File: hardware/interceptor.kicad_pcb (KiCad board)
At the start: 2 copper layers, 78.9 x 59.7 mm, 32 parts, among them IC1 ATMEGA1284P-P, K1 USB, P1 TAPEPORT, P2 CIA1, P3 KEYBOARD, P4 USER A, P5 USER B, SW1 RESET, SW2 BOOTLOADER, U1 7400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

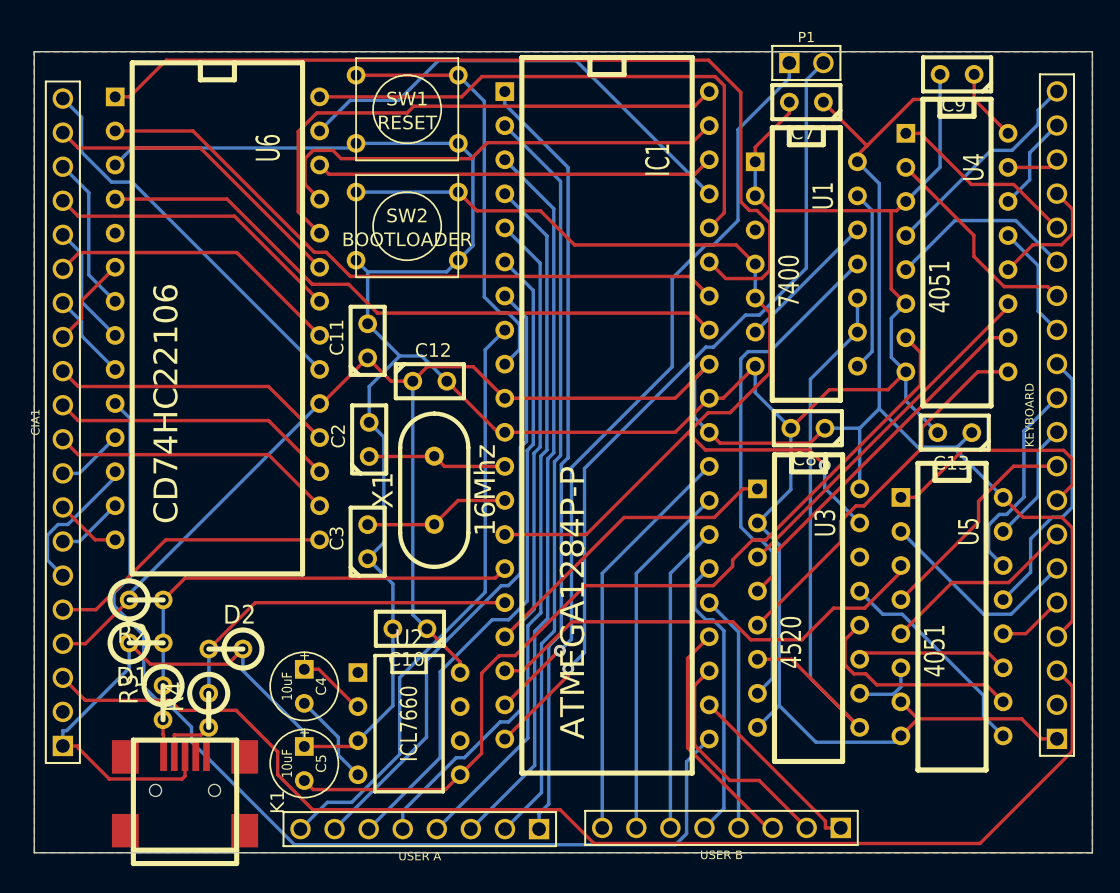
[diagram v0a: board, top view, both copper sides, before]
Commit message: Hardware: Fixed Crosspoint switch and usb connector, routed usb traces
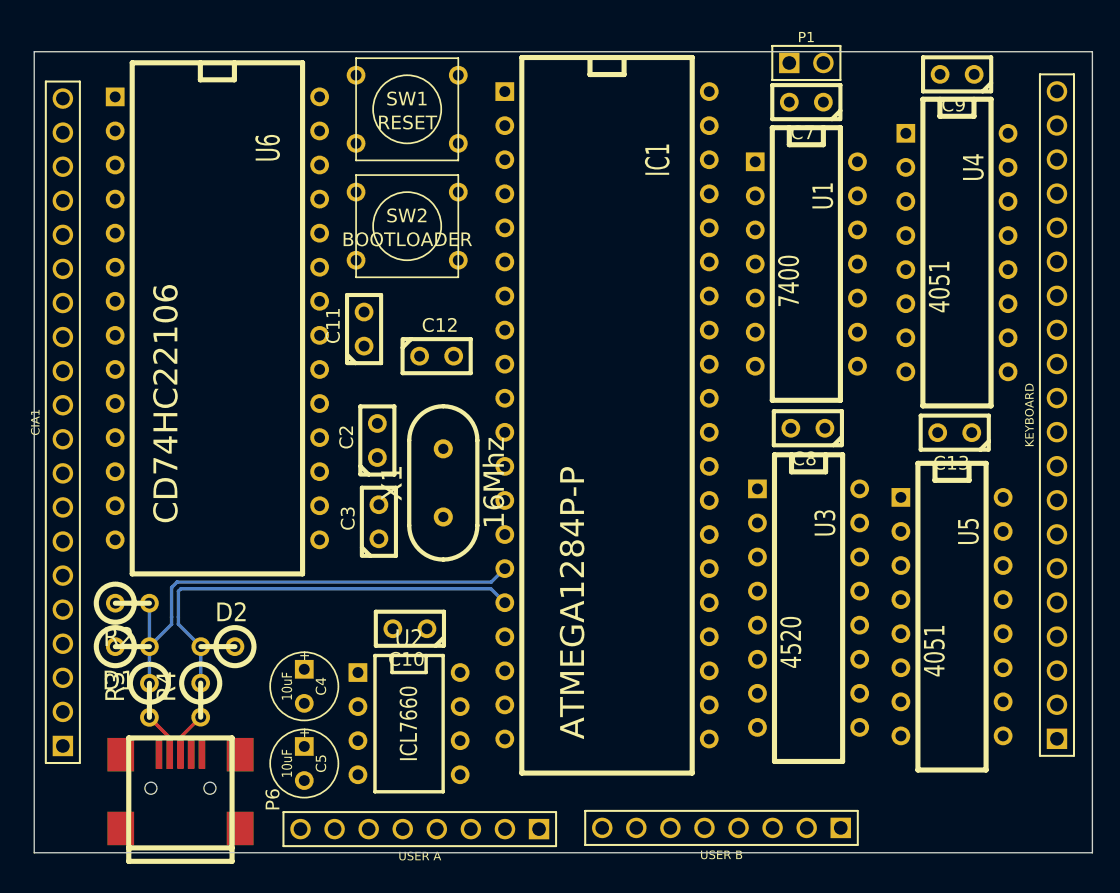
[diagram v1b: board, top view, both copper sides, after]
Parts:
- removed K1: USB, USB_MINI_B
- added P6: USB, USB_MINI_B_CORRECTED, F.Cu at (24.4, 88.6)
- moved C12 1.93 mm to (43.5, 55.5)
- moved C3 1.71 mm to (39.2, 67.9)
- moved D1 1.07 mm to (20.8, 77.2)
- moved R2 1.06 mm to (20.8, 73.9)
- moved R3 1.03 mm to (22.1, 81.2)
- moved R4 0.97 mm to (25.9, 81.2)
- moved C11 0.92 mm to (38.1, 53.5)
- moved X1 0.87 mm to (44.0, 65.0)
- moved D2 0.62 mm to (27.2, 77.2)
- moved C2 0.61 mm to (39.1, 61.8)
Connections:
- U6 pad 5: (no net) -> GND
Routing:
- net GND: track 280.1 -> 0.00 mm
- net VCC: track 176.6 -> 0.00 mm
- net /~RESTORE: track 90.7 -> 0.00 mm
- net /MR: track 81.9 -> 0.00 mm, vias 1 -> 0
- net /~CPMR: track 77.1 -> 0.00 mm
- net /CPA5: track 68.5 -> 0.00 mm
- net /VEE: track 66.5 -> 0.00 mm
- net /CD: track 61.2 -> 0.00 mm, vias 1 -> 0
- net /UA0: track 57.9 -> 0.00 mm
- net /CS: track 57.0 -> 0.00 mm, vias 1 -> 0
- net /UA1: track 55.9 -> 0.00 mm
- net /UA2: track 54.0 -> 0.00 mm
- net /UA3: track 52.1 -> 0.00 mm
- net /UA4: track 50.9 -> 0.00 mm
- net /~CPS: track 49.4 -> 0.00 mm
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- removed copper zone on B.Cu, net GND
- removed copper zone on F.Cu, net GND

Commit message: Hardware: First serious draft of pcb layout
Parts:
- removed C13, C7, C8, C9: 100nF, C1
- removed P5: USER B, pinHeader-8x1
- added JP1: JUMPER, PIN_ARRAY_2X1, F.Cu at (16.2, 89.1)
- C4, C5: footprint C1V5 -> CR2H11W5H
- P4: value USER A -> USER; footprint pinHeader-8x1 -> pin_array_8x2
- moved P1 57.6 mm to (57.0, 89.6), turned to 180 degrees
- moved P4 35.2 mm to (77.3, 86.9)
- moved R3 16.7 mm to (38.8, 80.9)
- moved D1 16.7 mm to (37.5, 76.9)
- moved D2 16.7 mm to (43.9, 76.9)
- moved P6 16.7 mm to (41.1, 88.3)
- moved R4 16.7 mm to (42.6, 80.9)
- moved R2 15.7 mm to (36.5, 73.4)
- moved C4 13.4 mm to (21.3, 85.2), turned to 180 degrees
- moved C10 12.5 mm to (29.4, 72.7)
- moved U2 12.3 mm to (29.5, 80.1)
- moved U5 6.50 mm to (83.0, 68.5)
- moved U3 5.82 mm to (72.0, 68.5)
- moved U1 5.25 mm to (72.0, 43.5)
- moved C5 4.30 mm to (31.0, 89.3)
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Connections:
- P2 pad 4: VCC -> /EXTVCC
- P3 pad 4: VCC -> (no net)
- P4 pad 2: /UA1 -> /UB0
- P4 pad 3: /UA2 -> /UA1
- P4 pad 4: /UA3 -> /UB1
- P4 pad 5: /UA4 -> /UA2
- P4 pad 6: /UA5 -> /UB2
- P4 pad 7: /UA6 -> /UA3
- P4 pad 8: /UA7 -> /UB3
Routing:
- net GND: track 0.00 -> 280.5 mm
- net VCC: track 0.00 -> 155.8 mm
- net /~RESTORE: track 0.00 -> 88.5 mm, vias 0 -> 1
- net /VEE: track 0.00 -> 84.8 mm, vias 0 -> 3
- net /MR: track 0.00 -> 83.7 mm, vias 0 -> 1
- net /UA0: track 0.00 -> 76.7 mm
- net /UA1: track 0.00 -> 71.8 mm
- net /MD: track 0.00 -> 70.6 mm
- net /UA2: track 0.00 -> 69.6 mm
- net /UA3: track 0.00 -> 65.0 mm
- net /UA4: track 0.00 -> 60.0 mm
- net /~CPMR: track 0.00 -> 55.6 mm
- net /UA5: track 0.00 -> 55.6 mm
- net /UA6: track 0.00 -> 52.9 mm
- net /~CPS: track 0.00 -> 50.3 mm
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- added copper zone on B.Cu, net GND
- added copper zone on F.Cu, net GND
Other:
- board size 78.9 x 59.7 mm -> 80 x 59.7 mm
- net class Power added: clearance 0.254, trace_width 0.508, via_dia 0.889, via_drill 0.635

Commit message: Hardware: Rerouted/Moved front copper traces around crystal to bottom layer
This prevents the metallic crystal casing from shorting traces on the
front layer in case the pcb has been made without solder mask.
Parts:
- moved C10 177.5 mm to (184.5, 158.9)
- moved C11 177.5 mm to (194.4, 142.8)
- moved C2 177.5 mm to (194.4, 148.5)
- moved C3 177.5 mm to (194.4, 154.1)
- moved C4 177.5 mm to (176.4, 171.5)
- moved C5 177.5 mm to (186.2, 175.5)
- moved D2 177.5 mm to (199.0, 163.1)
- moved IC1 177.5 mm to (212.0, 146.2)
- moved JP1 177.5 mm to (171.3, 175.4)
- moved P1 177.5 mm to (212.1, 175.8)
- moved P2 177.5 mm to (171.4, 146.7)
- moved P3 177.5 mm to (245.5, 146.1)
- moved P4 177.5 mm to (232.4, 173.2)
- moved P6 177.5 mm to (196.2, 174.5)
- moved R3 177.5 mm to (193.9, 167.1)
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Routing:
- net /~CPMR: track 55.6 -> 66.4 mm, vias 0 -> 1
- net GND: track 280.5 -> 275.5 mm
- net VCC: track 155.8 -> 156.9 mm

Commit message: Hardware: Improved routing around usb connector and other places
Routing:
- net /CPA5: track 50.3 -> 62.2 mm
- net /UA6: track 52.9 -> 64.5 mm
- net /UA0: track 76.7 -> 86.1 mm
- net /UA5: track 55.6 -> 64.6 mm
- net /MR: track 83.7 -> 91.6 mm
- net /CPA0: track 36.7 -> 44.2 mm
- net GND: track 275.5 -> 269.9 mm, vias 0 -> 1
- net VCC: track 156.9 -> 162.1 mm
- net /UA4: track 60.0 -> 64.4 mm
- net /CPA1: track 41.6 -> 44.6 mm
- net /~RESTORE: track 88.5 -> 90.5 mm, vias 1 -> 3
- net /B2: track 23.8 -> 25.7 mm
- net /C5: track 13.8 -> 15.4 mm
- net /CRES: track 36.2 -> 37.6 mm
- net /UB0: track 29.1 -> 30.5 mm
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
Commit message: Hardware: Revision 1
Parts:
- moved C3 81.4 mm to (130.4, 103.9)
- moved JP1 81.4 mm to (107.3, 125.2)
- moved U1 81.4 mm to (163.1, 79.5)
- moved C11 81.4 mm to (130.4, 92.6)
- moved C2 81.4 mm to (130.4, 98.3)
- moved IC1 81.4 mm to (147.9, 96.0)
- moved P1 81.4 mm to (148.1, 125.6)
- moved P6 81.4 mm to (132.2, 124.3)
- moved R3 81.4 mm to (129.9, 116.9)
- moved SW2 81.4 mm to (133.4, 83.8)
- moved U2 81.4 mm to (120.6, 116.1)
- moved U5 81.4 mm to (174.1, 104.6)
- moved C10 81.4 mm to (120.5, 108.8)
- moved C12 81.4 mm to (135.6, 93.3)
- moved C4 81.4 mm to (112.4, 121.3)
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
